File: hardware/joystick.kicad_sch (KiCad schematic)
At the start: 20 parts, among them J5 Joystick

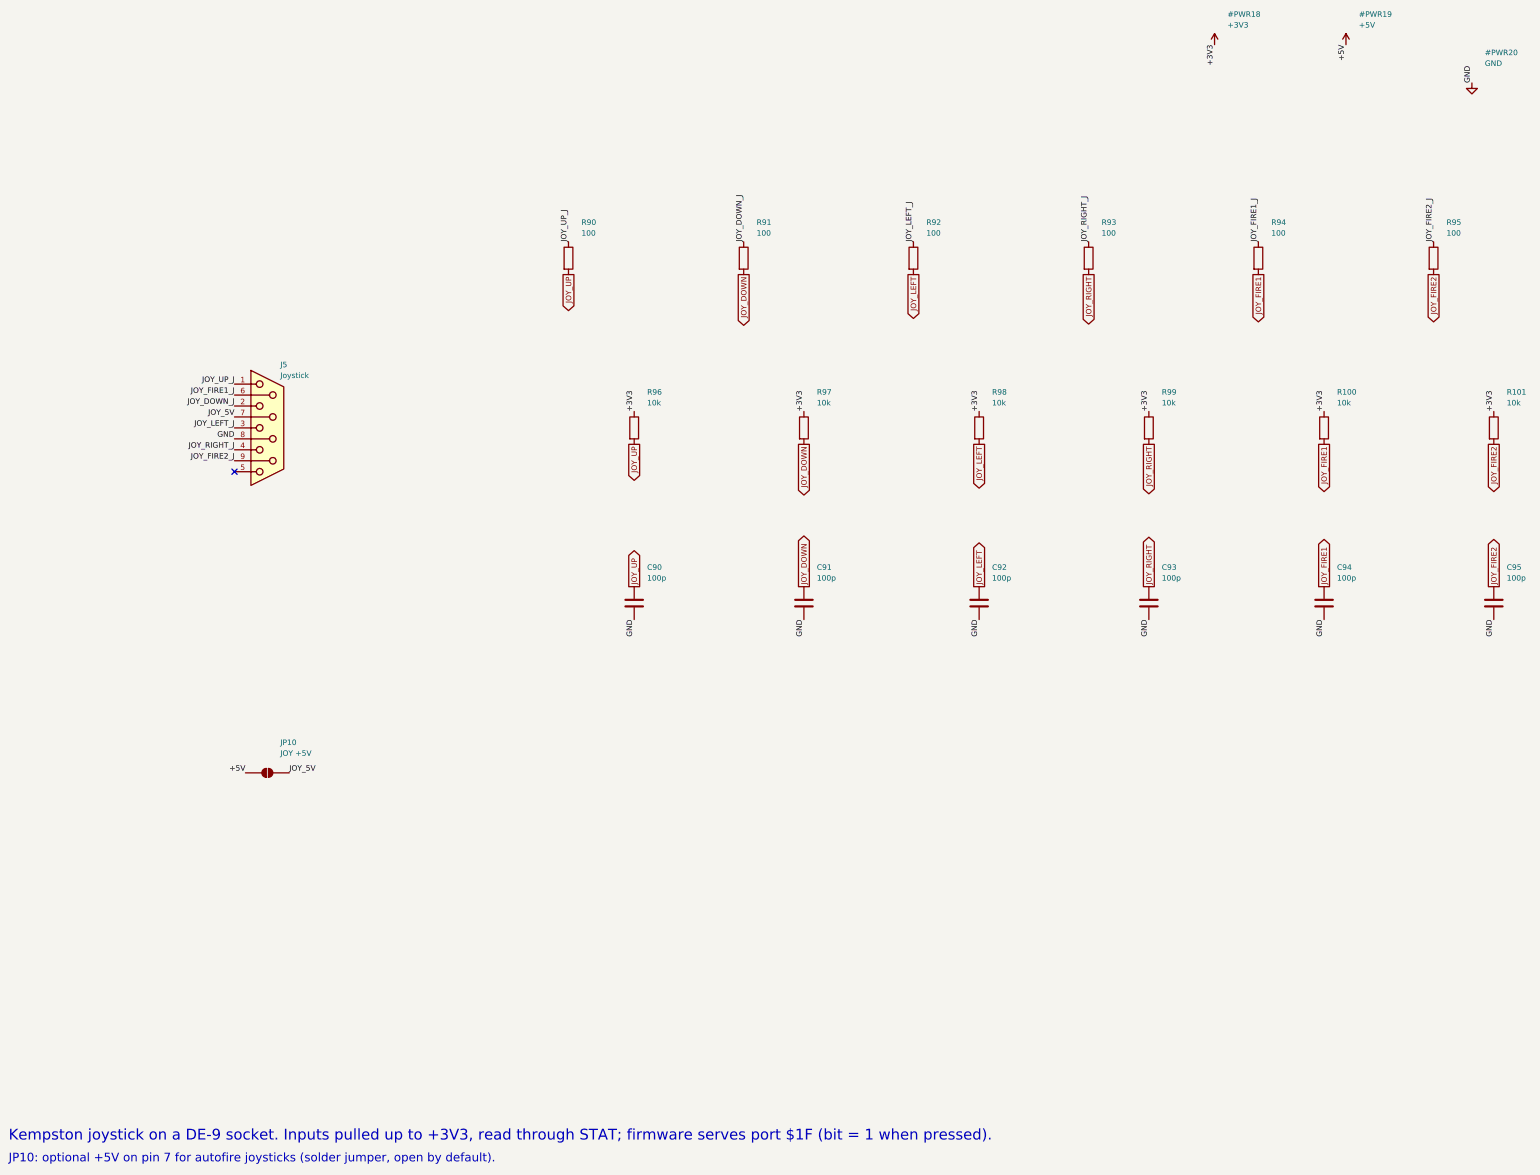
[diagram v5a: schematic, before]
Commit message: v3 proto3: male DE-9, I2C OLED header, buttons in a 2x2 block
- J5: male DE-9 (CONNFLY DS1037-09MNAKT74-0CC, C75750). Atari sticks end
  in a female plug; proto1/2's female footprint mirrors every pin under a
  male part, putting the stick's ground on pin 7 (JOY_5V, open), so nothing
  read. Same body position and mounting holes as proto2.
- J3: 1x4 header for a 1.54in 128x64 SSD1309 I2C module (1 GND, 2 +3V3,
  3 SCL GP43, 4 SDA GP42) on I2C1, R44/R45 4k7 pull-ups. Replaces the 7-pin
  SSD1351 SPI header; GP34, GP41 and expander P0.2 (with R11) are freed.
- SW3 under SW1, SW4 under SW2, so the module covers no buttons; D4/R5
  move left of the ESP32, between H1 and the USB-C socket.

Routed by flow.py on the first attempt: DRC clean at every severity,
2125 segments, 373 vias. ERC: the one existing U4 warning.

Co-Authored-By: Claude Opus 5.5 <noreply@anthropic.com>
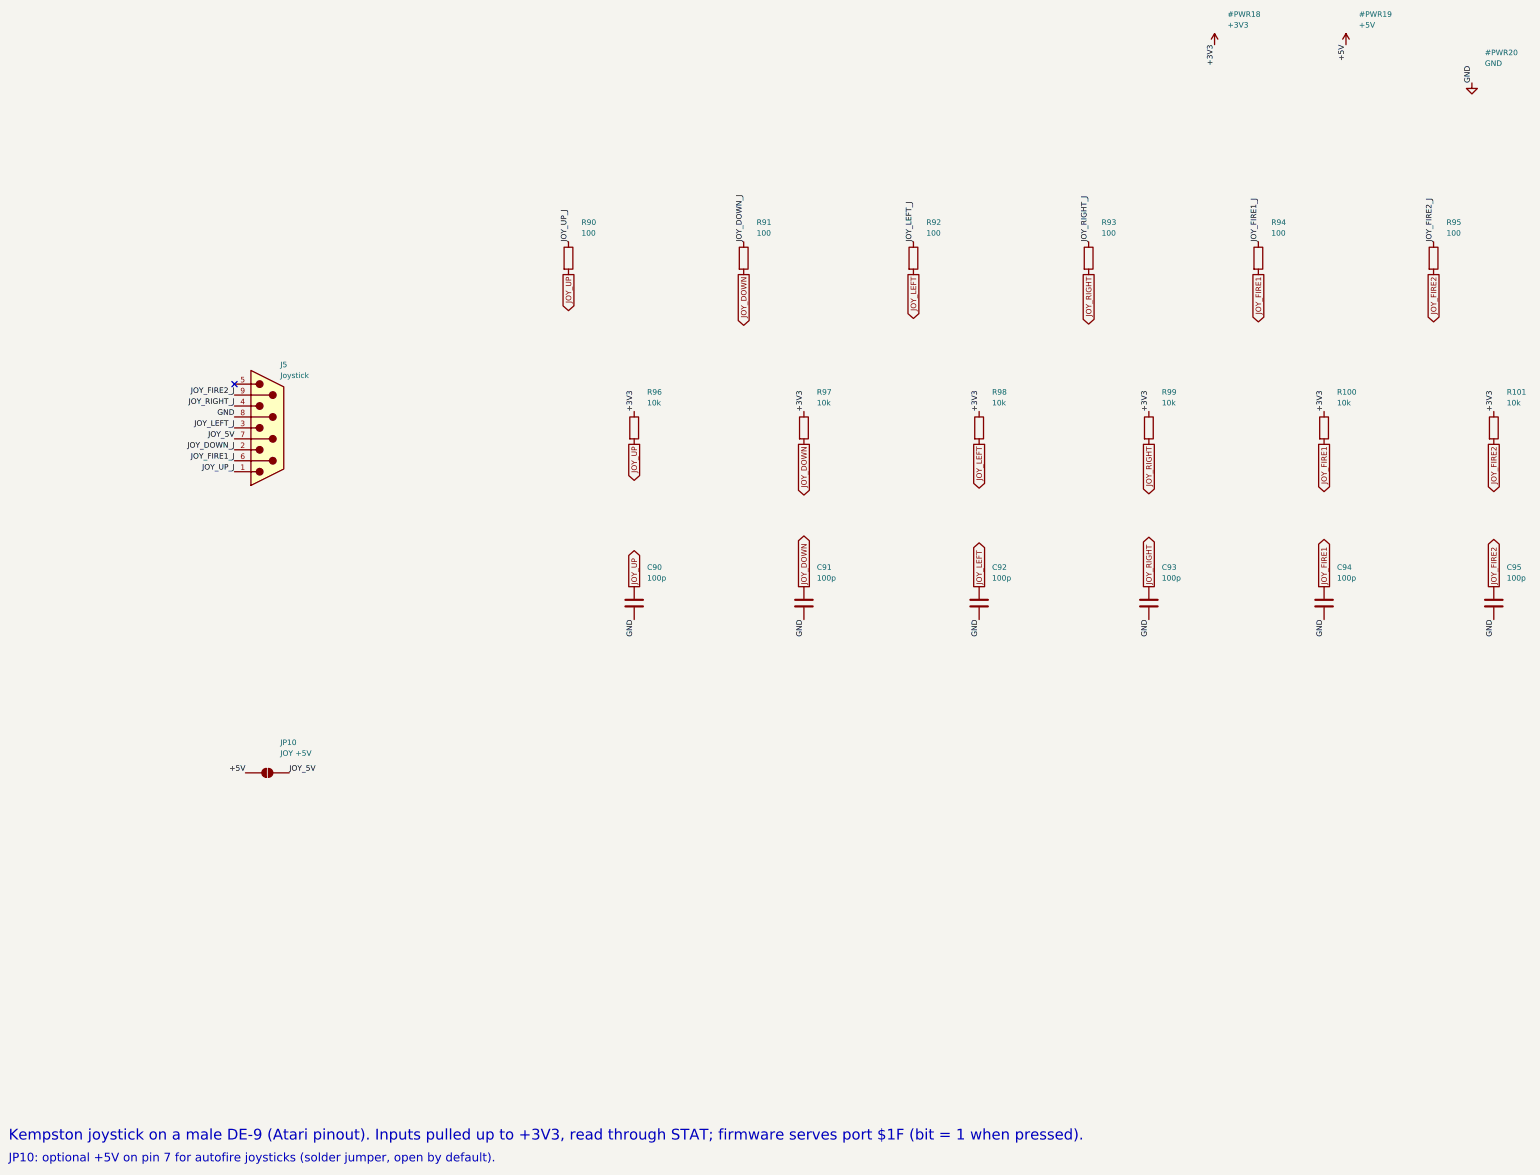
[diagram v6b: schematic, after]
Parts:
- removed J5: Joystick, Connector_Dsub:DSUB-9_Socket_Horizontal_P2.77x2.84mm_EdgePinOffset7.70mm_Housed_MountingHolesOffset9.12mm, symbol Connector:DE9_Socket
- added J5: Joystick, Connector_Dsub:DSUB-9_Pins_Horizontal_P2.77x2.84mm_EdgePinOffset7.70mm_Housed_MountingHolesOffset9.12mm, symbol Connector:DE9_Pins
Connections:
- net GND: now also J5.8
- net JOY_5V: now also J5.7
- net JOY_DOWN_J: now also J5.2
- net JOY_FIRE1_J: now also J5.6
- net JOY_FIRE2_J: now also J5.9
- net JOY_LEFT_J: now also J5.3
- net JOY_RIGHT_J: now also J5.4
- net JOY_UP_J: now also J5.1
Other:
- note added: "Kempston joystick on a male DE-9 (Atari pinout). Inputs pulled up to +3V3, read through STAT; firmware serves port $1F (bit = 1 when pressed)."
- note removed: "Kempston joystick on a DE-9 socket. Inputs pulled up to +3V3, read through STAT; firmware serves port $1F (bit = 1 when pressed)."
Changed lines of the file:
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@@
   (paper "A3")
   (title_block (title "TS-Pico v3: Joystick") (rev "0.1") (company "Timex/Sinclair Online User Group"))
-  (text "Kempston joystick on a DE-9 socket. Inputs pulled up to +3V3, read through STAT; firmware serves port $1F (bit = 1 when pressed)." (exclude_from_sim no) (at 20 285 0) (effects (font (size 2.5 2.5)) (justify left bottom)))
+  (text "Kempston joystick on a male DE-9 (Atari pinout). Inputs pulled up to +3V3, read through STAT; firmware serves port $1F (bit = 1 when pressed)." (exclude_from_sim no) (at 20 285 0) (effects (font (size 2.5 2.5)) (justify left bottom)))
   (text "JP10: optional +5V on pin 7 for autofire joysticks (solder jumper, open by default)." (exclude_from_sim no) (at 20 290 0) (effects (font (size 2.0 2.0)) (justify left bottom)))
   (symbol (lib_id "power:+3V3") (at 299.72 30.48 0) (unit 1)
@@
   )
   (label "GND" (at 359.41 39.37 90) (effects (font (size 1.27 1.27)) (justify left bottom)))
-  (symbol (lib_id "Connector:DE9_Socket") (at 80.01 119.38 0) (unit 1)
+  (symbol (lib_id "Connector:DE9_Pins") (at 80.01 119.38 0) (unit 1)
     (exclude_from_sim no) (in_bom yes) (on_board yes) (dnp no)
     (property "Reference" "J5" (at 83.01 104.72 0) (effects (font (size 1.27 1.27)) (justify left)))
     (property "Value" "Joystick" (at 83.01 107.22 0) (effects (font (size 1.27 1.27)) (justify left)))
-    (property "Footprint" "Connector_Dsub:DSUB-9_Socket_Horizontal_P2.77x2.84mm_EdgePinOffset7.70mm_Housed_MountingHolesOffset9.12mm" (at 80.01 119.38 0) (effects (font (size 1.27 1.27)) (justify left) (hide yes)))
+    (property "Footprint" "Connector_Dsub:DSUB-9_Pins_Horizontal_P2.77x2.84mm_EdgePinOffset7.70mm_Housed_MountingHolesOffset9.12mm" (at 80.01 119.38 0) (effects (font (size 1.27 1.27)) (justify left) (hide yes)))
     (property "Datasheet" "" (at 80.01 119.38 0) (effects (font (size 1.27 1.27)) (justify left) (hide yes)))
     (property "Description" "" (at 80.01 119.38 0) (effects (font (size 1.27 1.27)) (justify left) (hide yes)))
-    (property "MPN" "DS1037-09FNAKT74-0CC" (at 80.01 119.38 0) (effects (font (size 1.27 1.27)) (justify left) (hide yes)))
-    (property "LCSC" "C75749" (at 80.01 119.38 0) (effects (font (size 1.27 1.27)) (justify left) (hide yes)))
+    (property "MPN" "DS1037-09MNAKT74-0CC" (at 80.01 119.38 0) (effects (font (size 1.27 1.27)) (justify left) (hide yes)))
+    (property "LCSC" "C75750" (at 80.01 119.38 0) (effects (font (size 1.27 1.27)) (justify left) (hide yes)))
     (pin "1")
     (pin "2")
@@
     (instances (project "tspico-v3" (path "/9088d141-8624-4d5c-91a9-7a3a7a90b3cc/478bcdc2-09a7-4c3e-8209-8cd988b12aeb" (reference "J5") (unit 1))))
   )
-  (label "JOY_UP_J" (at 72.39 109.22 180) (effects (font (size 1.27 1.27)) (justify right bottom)))
-  (label "JOY_DOWN_J" (at 72.39 114.30 180) (effects (font (size 1.27 1.27)) (justify right bottom)))
+  (label "JOY_UP_J" (at 72.39 129.54 180) (effects (font (size 1.27 1.27)) (justify right bottom)))
+  (label "JOY_DOWN_J" (at 72.39 124.46 180) (effects (font (size 1.27 1.27)) (justify right bottom)))
   (label "JOY_LEFT_J" (at 72.39 119.38 180) (effects (font (size 1.27 1.27)) (justify right bottom)))
-  (label "JOY_RIGHT_J" (at 72.39 124.46 180) (effects (font (size 1.27 1.27)) (justify right bottom)))
-  (label "JOY_FIRE1_J" (at 72.39 111.76 180) (effects (font (size 1.27 1.27)) (justify right bottom)))
-  (label "JOY_FIRE2_J" (at 72.39 127.00 180) (effects (font (size 1.27 1.27)) (justify right bottom)))
-  (label "GND" (at 72.39 121.92 180) (effects (font (size 1.27 1.27)) (justify right bottom)))
-  (label "JOY_5V" (at 72.39 116.84 180) (effects (font (size 1.27 1.27)) (justify right bottom)))
-  (no_connect (at 72.39 129.54))
+  (label "JOY_RIGHT_J" (at 72.39 114.30 180) (effects (font (size 1.27 1.27)) (justify right bottom)))
+  (label "JOY_FIRE1_J" (at 72.39 127.00 180) (effects (font (size 1.27 1.27)) (justify right bottom)))
+  (label "JOY_FIRE2_J" (at 72.39 111.76 180) (effects (font (size 1.27 1.27)) (justify right bottom)))
+  (label "GND" (at 72.39 116.84 180) (effects (font (size 1.27 1.27)) (justify right bottom)))
+  (label "JOY_5V" (at 72.39 121.92 180) (effects (font (size 1.27 1.27)) (justify right bottom)))
+  (no_connect (at 72.39 109.22))
   (symbol (lib_id "Device:R") (at 149.86 80.01 0) (unit 1)
     (exclude_from_sim no) (in_bom yes) (on_board yes) (dnp no)
